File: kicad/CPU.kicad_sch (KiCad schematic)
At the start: 30 parts, among them SW1 SW_Push, U10 MC34063AD, U11 LD1117S33TR_SOT223, U5 STM32F303CBTx, X1 8 MHz

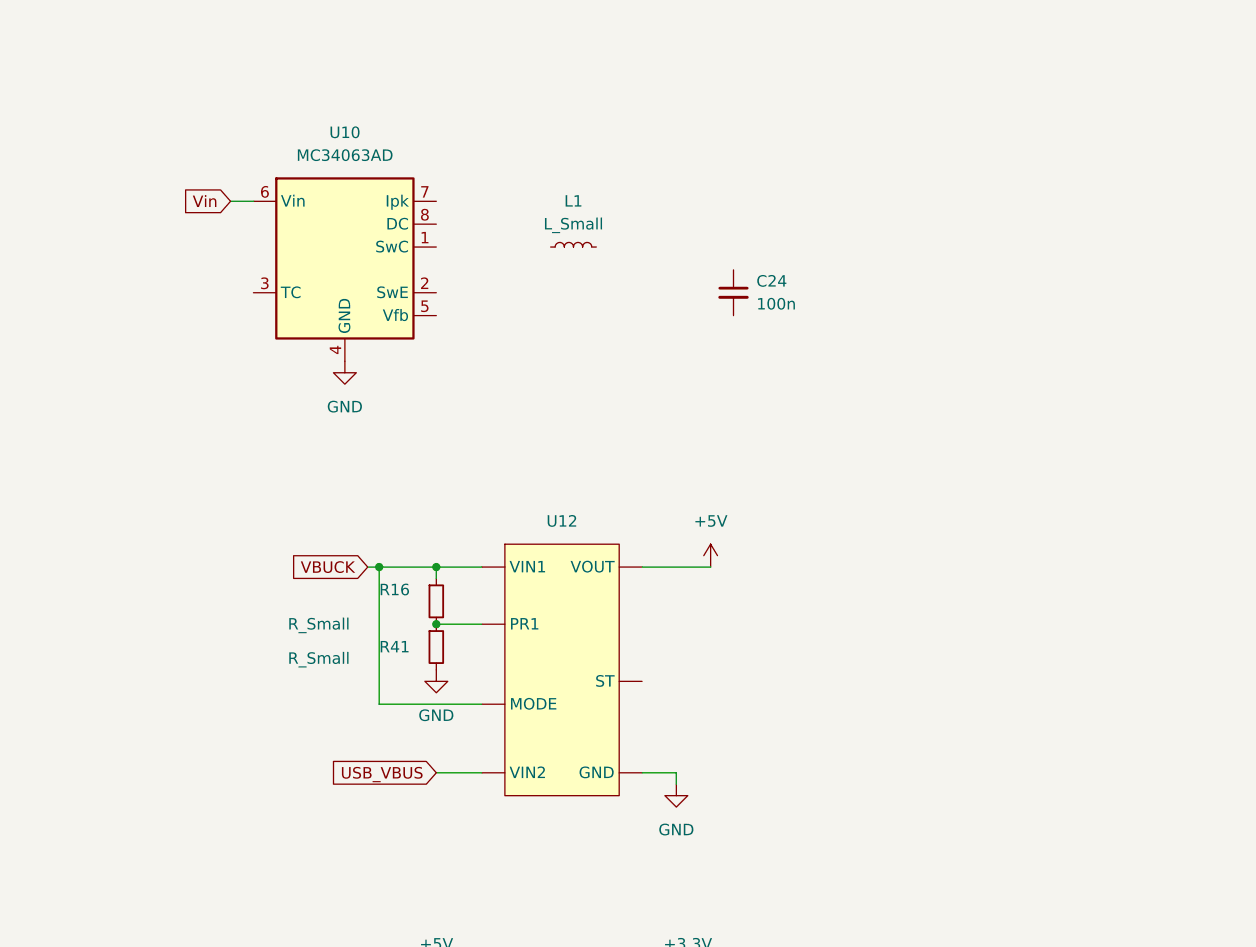
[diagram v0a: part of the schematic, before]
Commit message: [kicad] Added capacitor to buck circuit, added netlabels | TODO: Add pi-filter to usb-c output, add additional 5 V regulator to buck-circuit output with good noise rejection ratio
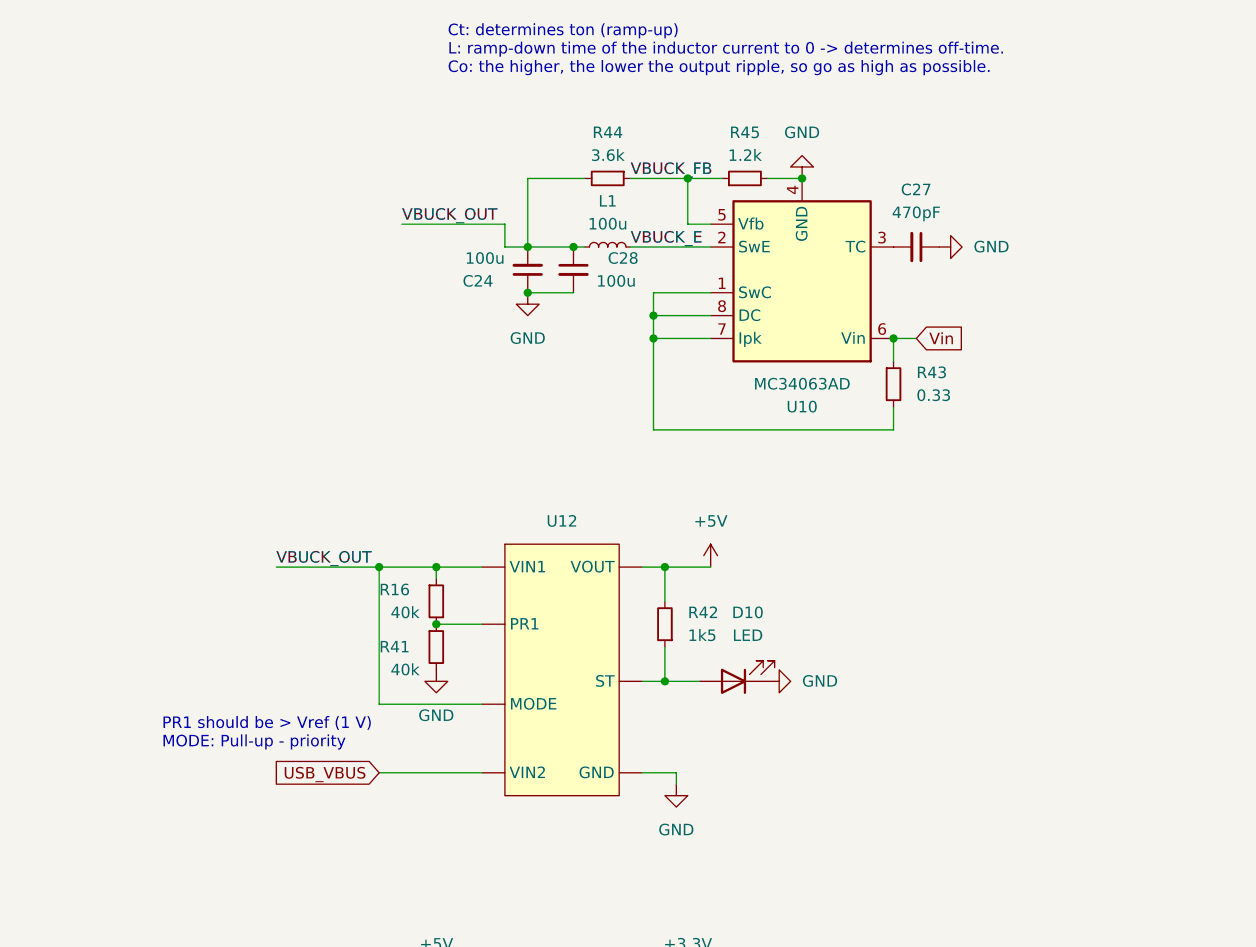
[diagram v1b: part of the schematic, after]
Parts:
- added C27: 470pF, Capacitor_SMD:C_0603_1608Metric, symbol Device:C_Small
- added C28: 100u, Capacitor_SMD:C_1210_3225Metric, symbol Device:C_Small
- added D10: LED, LED_SMD:LED_0805_2012Metric, symbol Device:LED
- added R42: 1k5, symbol Device:R_Small
- added R43: 0.33, symbol Device:R_Small
- added R44: 3.6k, symbol Device:R_Small
- added R45: 1.2k, symbol Device:R_Small
- C24: value 100n -> 100u; footprint (none) -> Capacitor_SMD:C_1210_3225Metric
- L1: value L_Small -> 100u; footprint (none) -> Inductor_SMD:L_1210_3225Metric
- R16, R41: value R_Small -> 40k
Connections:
- net VBUCK is gone; now on net VBUCK_OUT: R16.1, U12. (VOUT)
- net +5V: now also R42.2
- net GND: now also C24.1, C27.1, C28.2, D10.1 (K), R45.2
- net Vin: now also R43.1
- net VBUCK_OUT: now reaches U12. (VOUT)
- net VBUCK_OUT: now also C24.2, L1.1, C28.1, R44.2
- net at U10.1 (SwC): now also U10.7 (Ipk), U10.8 (DC), R43.2
- net VBUCK_E: now reaches U10.2 (SwE)
- net VBUCK_E: now also L1.2
- net at U10.3 (TC): now also C27.2
- net VBUCK_FB: now reaches U10.5 (Vfb)
- net VBUCK_FB: now also R44.1, R45.1
- new net: D10.2 (A), R42.1, U12. (VOUT)
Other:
- note added: "Ct: determines ton (ramp-up) L: ramp-down time of the inductor current to 0 -> determines off-time. Co: the higher, the lower the output ripple, so go as high as possible."
- note added: "PR1 should be > Vref (1 V) MODE: Pull-up - priority"
- moved on the sheet: C24, L1, U10

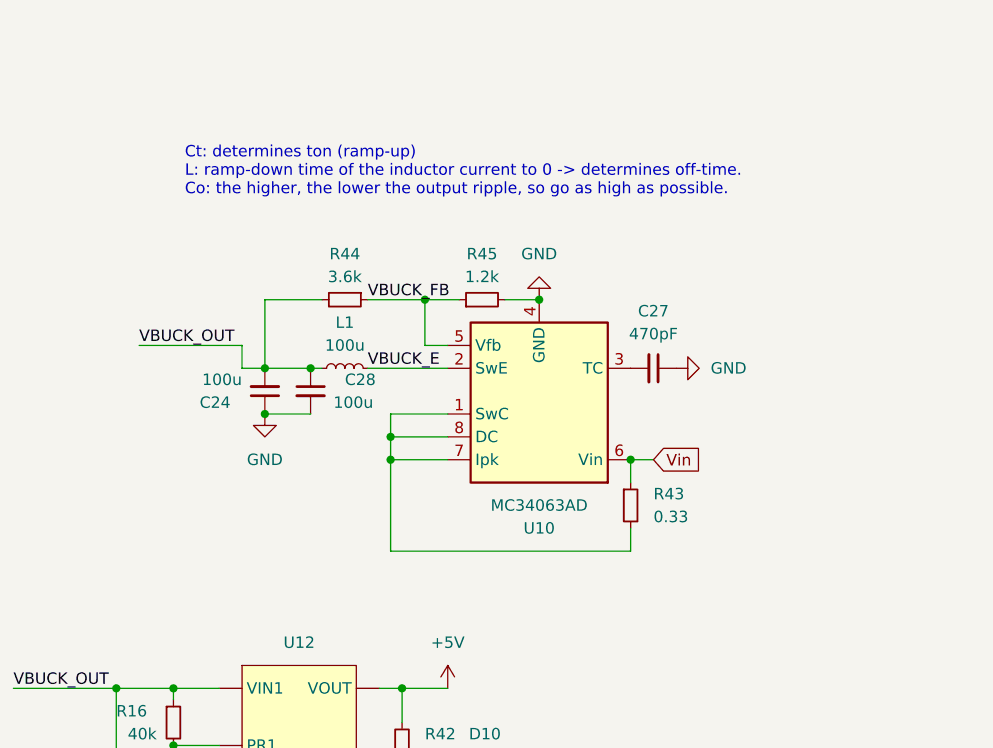
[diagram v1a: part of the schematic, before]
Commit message: [kicad] input capacitance added [simulations] added ferrite simulation
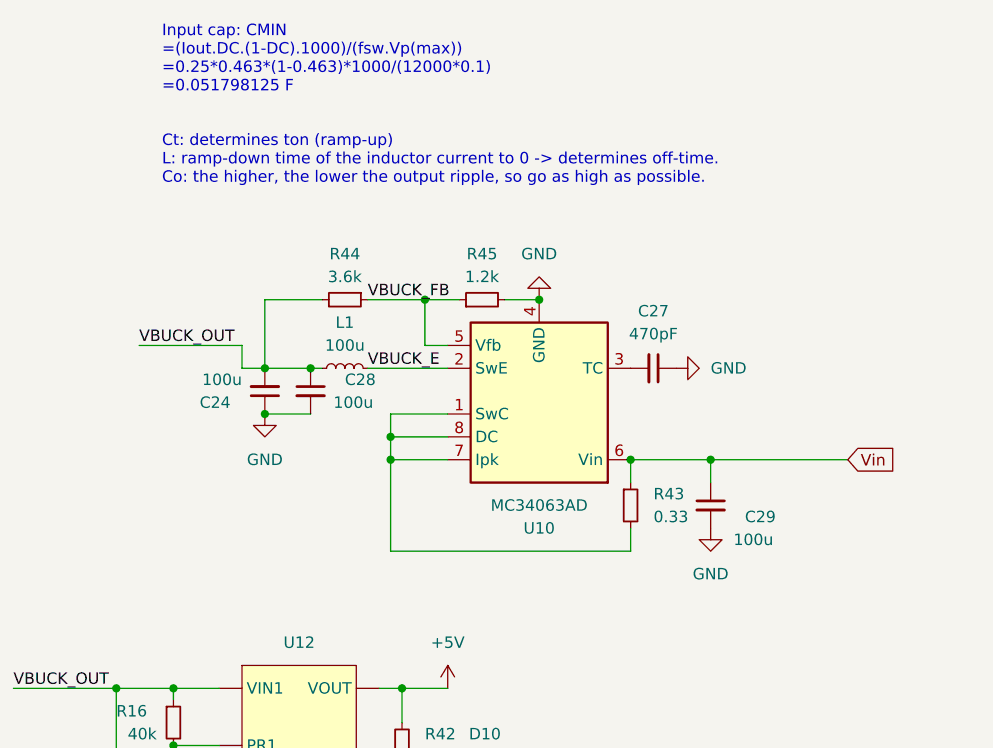
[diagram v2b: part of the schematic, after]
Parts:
- added C29: 100u, Capacitor_SMD:C_1210_3225Metric, symbol Device:C_Small
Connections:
- net GND: now also C29.2
- net Vin: now also C29.1
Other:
- note added: "Input cap: CMIN =(Iout.DC.(1-DC).1000)/(fsw.Vp(max)) =0.25*0.463*(1-0.463)*1000/(12000*0.1) =0.051798125 F"
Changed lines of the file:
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@@
   (junction (at 49.53 124.46) (diameter 0) (color 0 0 0 0)
   )
+  (junction (at 256.54 38.1) (diameter 0) (color 0 0 0 0)
+  )
   (junction (at 40.64 41.91) (diameter 0) (color 0 0 0 0)
   )
@@
     (stroke (width 0) (type default))
   )
+  (wire (pts (xy 256.54 38.1) (xy 247.65 38.1))
+    (stroke (width 0) (type default))
+  )
   (wire (pts (xy 38.1 72.39) (xy 46.99 72.39))
     (stroke (width 0) (type default))
@@
     (stroke (width 0) (type default))
   )
+  (wire (pts (xy 256.54 40.64) (xy 256.54 38.1))
+    (stroke (width 0) (type default))
+  )
   (wire (pts (xy 224.79 113.03) (xy 224.79 115.57))
     (stroke (width 0) (type default))
@@
     (stroke (width 0) (type default))
   )
-  (wire (pts (xy 250.19 38.1) (xy 247.65 38.1))
+  (wire (pts (xy 271.78 38.1) (xy 256.54 38.1))
     (stroke (width 0) (type default))
   )
@@
   )
   (text "Ct: determines ton (ramp-up)\nL: ramp-down time of the inductor current to 0 -> determines off-time.\nCo: the higher, the lower the output ripple, so go as high as possible."
-    (at 198.12 8.89 0)
+    (at 195.58 7.62 0)
+    (effects (font (size 1.27 1.27)) (justify left bottom))
+  )
+  (text "Input cap: CMIN\n=(Iout.DC.(1-DC).1000)/(fsw.Vp(max))\n=0.25*0.463*(1-0.463)*1000/(12000*0.1)\n=0.051798125 F"
+    (at 195.58 -2.54 0)
     (effects (font (size 1.27 1.27)) (justify left bottom))
   )
@@
     )
   )
-  (global_label "Vin" (shape input) (at 250.19 38.1 0) (fields_autoplaced)
+  (global_label "Vin" (shape input) (at 271.78 38.1 0) (fields_autoplaced)
     (effects (font (size 1.27 1.27)) (justify left))
-    (property "Intersheetrefs" "${INTERSHEET_REFS}" (at 256.0176 38.1 0)
+    (property "Intersheetrefs" "${INTERSHEET_REFS}" (at 277.6076 38.1 0)
       (effects (font (size 1.27 1.27)) (justify left) hide)
     )
@@
     )
   )
+  (symbol (lib_id "power:GND") (at 256.54 45.72 0) (unit 1)
+    (in_bom yes) (on_board yes) (dnp no) (fields_autoplaced)
+    (property "Reference" "#PWR057" (at 256.54 52.07 0)
+      (effects (font (size 1.27 1.27)) hide)
+    )
+    (property "Value" "GND" (at 256.54 50.8 0)
+      (effects (font (size 1.27 1.27)))
+    )
+    (property "Footprint" "" (at 256.54 45.72 0)
+      (effects (font (size 1.27 1.27)) hide)
+    )
+    (property "Datasheet" "" (at 256.54 45.72 0)
+      (effects (font (size 1.27 1.27)) hide)
+    )
+    (pin "1")
+    (instances
+      (project "bldc_project"
+        (path "/91e2f46a-700b-4d7a-a06a-22469f63223f/7eb1e86b-8a48-408f-b231-0c52f4ea1971"
+          (reference "#PWR057") (unit 1)
+        )
+      )
+    )
+  )
   (symbol (lib_id "Device:C_Small") (at 250.19 27.94 270) (unit 1)
     (in_bom yes) (on_board yes) (dnp no) (fields_autoplaced)
@@
         )
       )
+    )
+  )
+  (symbol (lib_id "Device:C_Small") (at 256.54 43.18 0) (unit 1)
+    (in_bom yes) (on_board yes) (dnp no)
+    (property "Reference" "C29" (at 260.35 44.45 0)
+      (effects (font (size 1.27 1.27)) (justify left))
+    )
+    (property "Value" "100u" (at 259.08 46.99 0)
+      (effects (font (size 1.27 1.27)) (justify left))
+    )
+    (property "Footprint" "Capacitor_SMD:C_1210_3225Metric" (at 256.54 43.18 0)
+      (effects (font (size 1.27 1.27)) hide)
+    )
+    (property "Datasheet" "https://wmsc.lcsc.com/wmsc/upload/file/pdf/v2/lcsc/2304140030_Hunan-Xiangyee-in-S-T-CA55-B6R3M107T_C568913.pdf" (at 256.54 43.18 0)
+      (effects (font (size 1.27 1.27)) hide)
+    )
+    (pin "2")
+    (pin "1")
+    (instances
+      (project "bldc_project"
+        (path "/91e2f46a-700b-4d7a-a06a-22469f63223f/7eb1e86b-8a48-408f-b231-0c52f4ea1971"
+          (reference "C29") (unit 1)
+        )
+      )

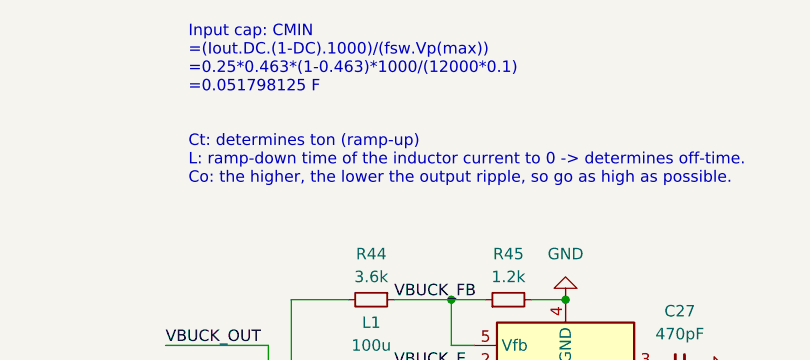
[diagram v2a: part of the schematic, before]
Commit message: brought some order in filter simulations
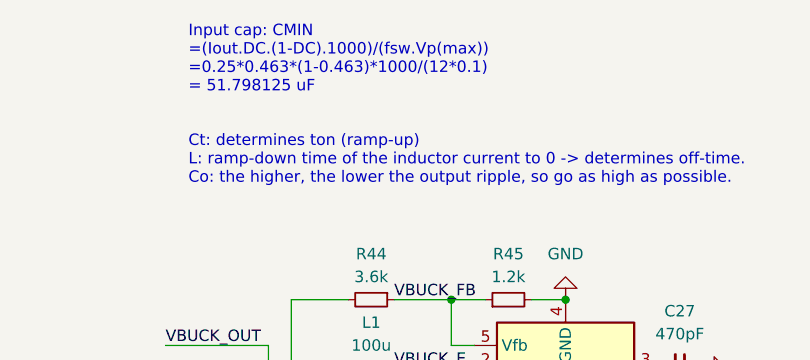
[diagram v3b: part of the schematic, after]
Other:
- note added: "Input cap: CMIN =(Iout.DC.(1-DC).1000)/(fsw.Vp(max)) =0.25*0.463*(1-0.463)*1000/(12*0.1) = 51.798125 uF"
- note removed: "Input cap: CMIN =(Iout.DC.(1-DC).1000)/(fsw.Vp(max)) =0.25*0.463*(1-0.463)*1000/(12000*0.1) =0.051798125 F"
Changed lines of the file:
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@@
     (effects (font (size 1.27 1.27)) (justify left bottom))
   )
-  (text "Input cap: CMIN\n=(Iout.DC.(1-DC).1000)/(fsw.Vp(max))\n=0.25*0.463*(1-0.463)*1000/(12000*0.1)\n=0.051798125 F"
+  (text "Input cap: CMIN\n=(Iout.DC.(1-DC).1000)/(fsw.Vp(max))\n=0.25*0.463*(1-0.463)*1000/(12*0.1)\n= 51.798125 uF"
     (at 195.58 -2.54 0)
     (effects (font (size 1.27 1.27)) (justify left bottom))
